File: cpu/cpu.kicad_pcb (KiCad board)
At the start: 4 copper layers, 102.4 x 40.3 mm, 39 parts, among them J2 Conn_01x08, Q3 RU1J002YN, U1 ICE40HX1K-VQ100_RV4028, U2 W25Q80DVSS, U3 AP2112K-1.2

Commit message: RAM module, many tweaks
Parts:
- Q3: value RU1J002YN -> 2N7002; footprint Package_TO_SOT_SMD:SOT-323_SC-70 -> Package_TO_SOT_SMD:SOT-23
- moved Q3 0.22 mm to (116.6, 83.4)
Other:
- board text added: "LED"
- board text added: "PROG"

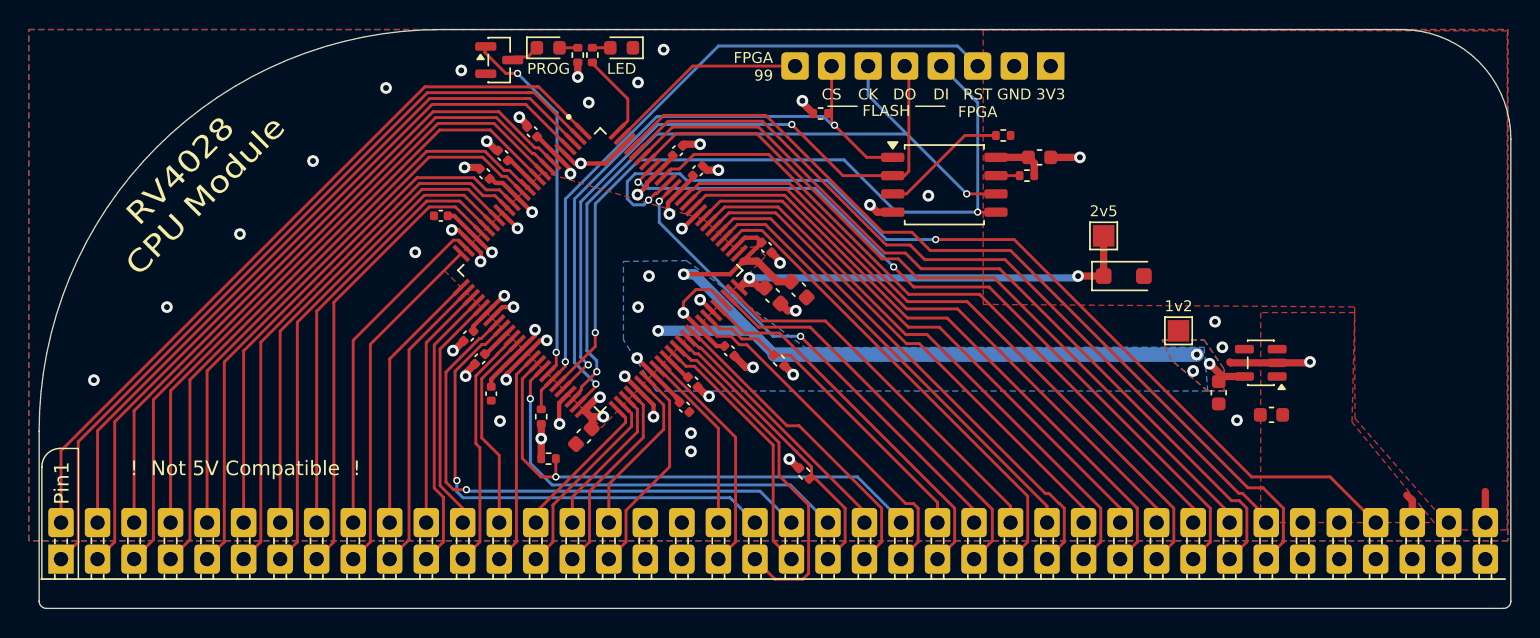
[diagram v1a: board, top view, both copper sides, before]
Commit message: Relayout CPU
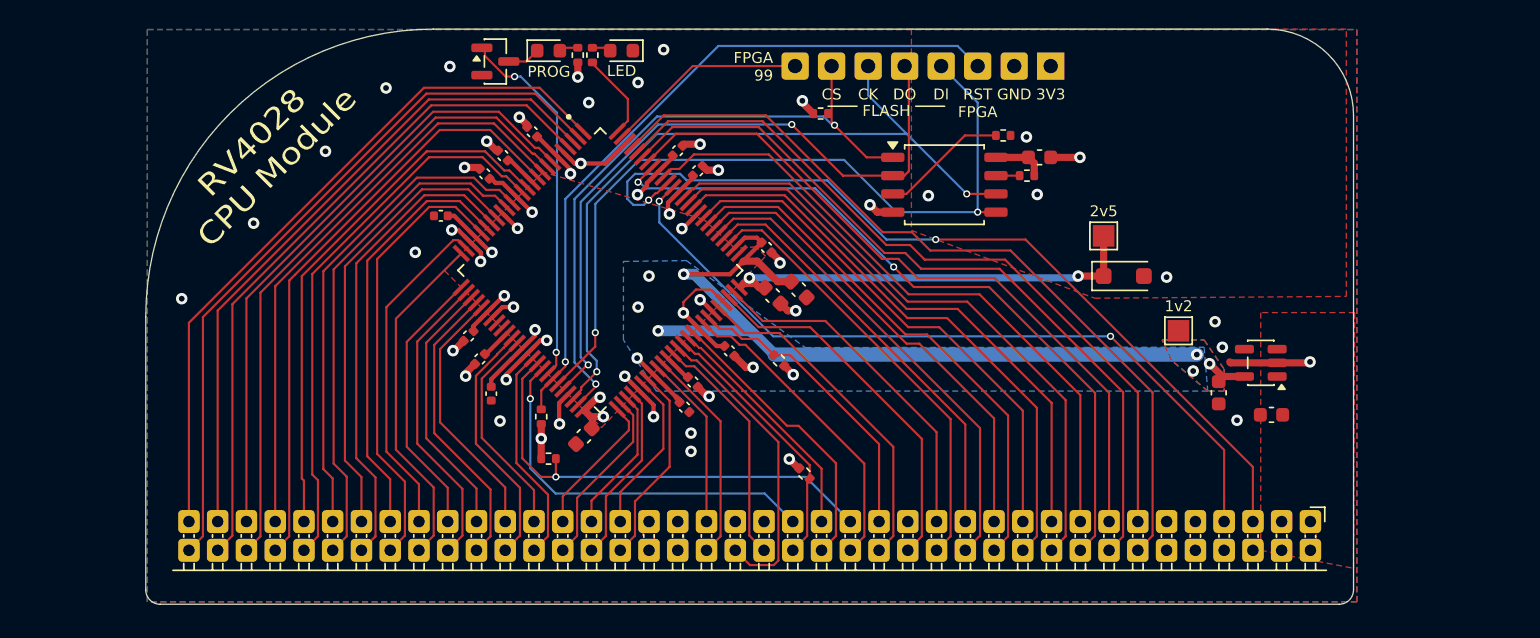
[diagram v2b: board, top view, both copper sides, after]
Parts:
- J1: footprint RV4028:ModuleHeader -> RV4028:Module_2mm
- moved J1 1.41 mm to (134.0, 117.0)
- moved Q3 0.29 mm to (116.3, 83.5)
- moved D3 0.20 mm to (120.0, 82.8)
- moved D2 0.20 mm to (125.1, 82.8)
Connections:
- J1 pad 18: unconnected-(J1-PWR-Pad18) -> +3V3
- J1 pad 40: +3V3 -> +5V
- J1 pad 58: unconnected-(J1-PWR-Pad58) -> +3V3
- J1 pad 60: ~{RST2} -> GND
- J1 pad 61: CLK2 -> GND
- J1 pad 66: SPARE1 -> GND
- J1 pad 77: SPARE2 -> SPARE1
- J1 pad 78: +5V -> SPARE2
- J1 pad 80: +3V3 -> +5V
- U1 pad 33: CLK2 -> unconnected-(U1-CLK2-Pad33)
- U1 pad 34: ~{RST2} -> unconnected-(U1-~{RST2}-Pad34)
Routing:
- net CLK2: track 37.8 -> 0.00 mm, vias 1 -> 0
- net ~{RST2}: track 34.5 -> 0.00 mm, vias 1 -> 0
- net SPARE1: track 33.9 -> 53.7 mm
- net +3V3: track 60.9 -> 53.8 mm, vias 16 -> 19
- net SPARE2: track 67.2 -> 60.8 mm
- net D7: track 61.5 -> 56.5 mm
- net D6: track 57.9 -> 53.3 mm
- net A30: track 54.7 -> 50.4 mm
- net A29: track 51.9 -> 47.8 mm
- net D5: track 54.7 -> 50.7 mm
- net D15: track 56.4 -> 52.5 mm
- net A28: track 48.6 -> 44.8 mm
- net D4: track 47.9 -> 44.1 mm
- net A31: track 53.1 -> 49.3 mm
- net ~{BUSRQ}: track 36.6 -> 32.9 mm
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- added copper zone on B.Cu, net +5V
- added copper zone on In1.Cu, net +5V
- added copper zone on In2.Cu, net +5V
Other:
- board size 102.4 x 40.3 mm -> 84 x 40 mm
- board text added: "J1"
- board text removed: "! Not 5V Compatible !"

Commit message: IO module 2mm headers
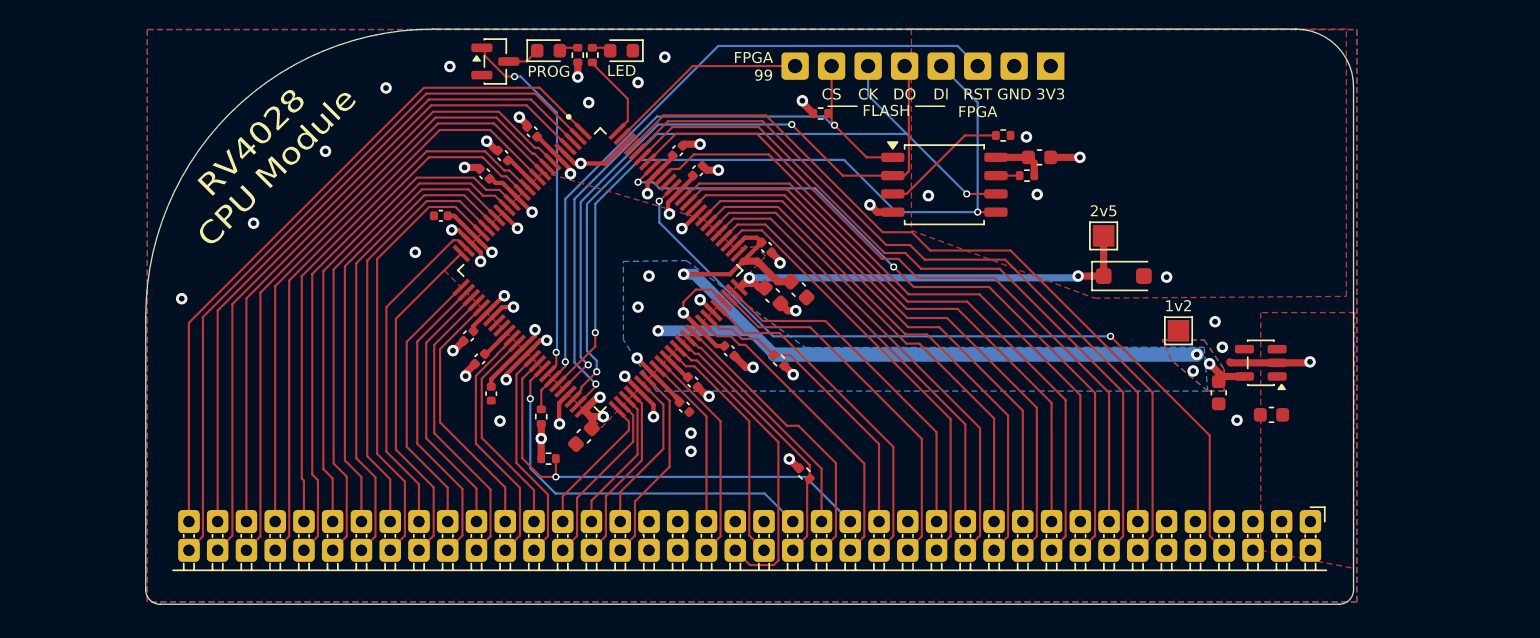
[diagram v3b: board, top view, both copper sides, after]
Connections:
- J1 pad 37: unconnected-(J1-USB_DP-Pad37) -> SPARE1
- J1 pad 77: SPARE1 -> unconnected-(J1-USB_DN-Pad77)
- J1 pad 78: SPARE2 -> unconnected-(J1-USB_DP-Pad78)
- U1 pad 90: SPARE2 -> unconnected-(U1-SPARE2-Pad90)
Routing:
- net SPARE2: track 60.8 -> 0.00 mm, vias 2 -> 0
- net SPARE1: track 53.7 -> 55.7 mm
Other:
- outline, holes or cut-outs redrawn
- board text added: "RV2048 CPU v0.1 © Mike Bell 2026 JLCJLCJLCJLC"

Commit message: RAM board attempt 2
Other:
- board text added: "RV2048 CPU v0.1 © Michael Bell 2026 JLCJLCJLCJLC"
- board text removed: "RV2048 CPU v0.1 © Mike Bell 2026 JLCJLCJLCJLC"
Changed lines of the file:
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@@
 		)
 	)
-	(gr_text "RV2048 CPU v0.1\n© Mike Bell 2026\nJLCJLCJLCJLC"
+	(gr_text "RV2048 CPU v0.1\n© Michael Bell 2026\nJLCJLCJLCJLC"
 		(at 175 101.25 90)
 		(layer "B.SilkS")

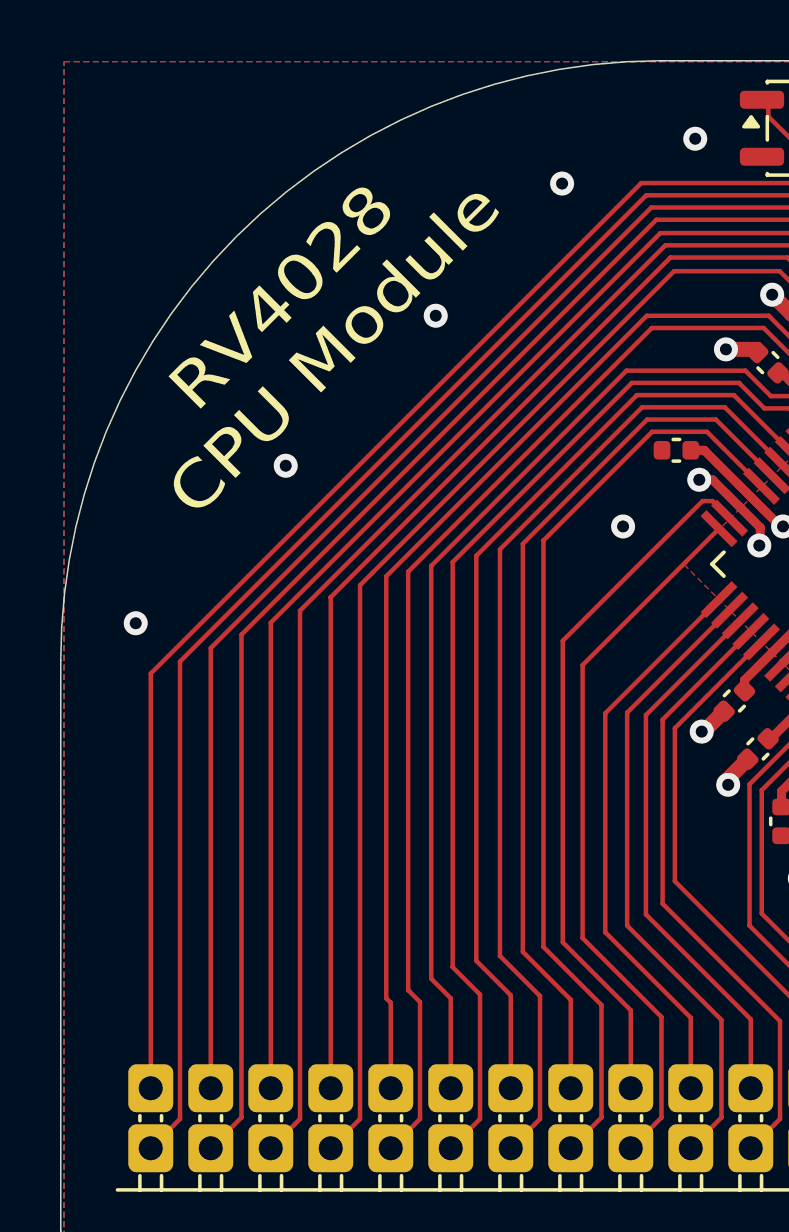
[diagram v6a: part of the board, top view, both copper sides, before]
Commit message: Finish RAM module routing
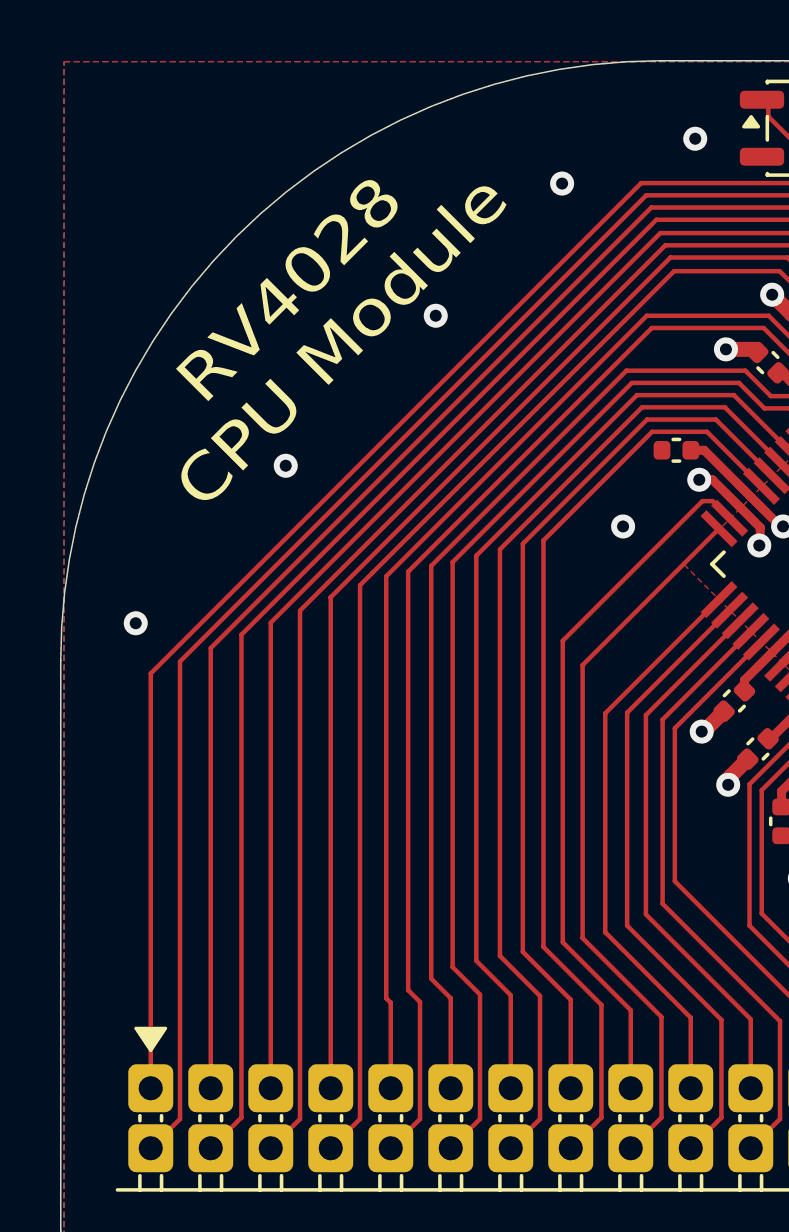
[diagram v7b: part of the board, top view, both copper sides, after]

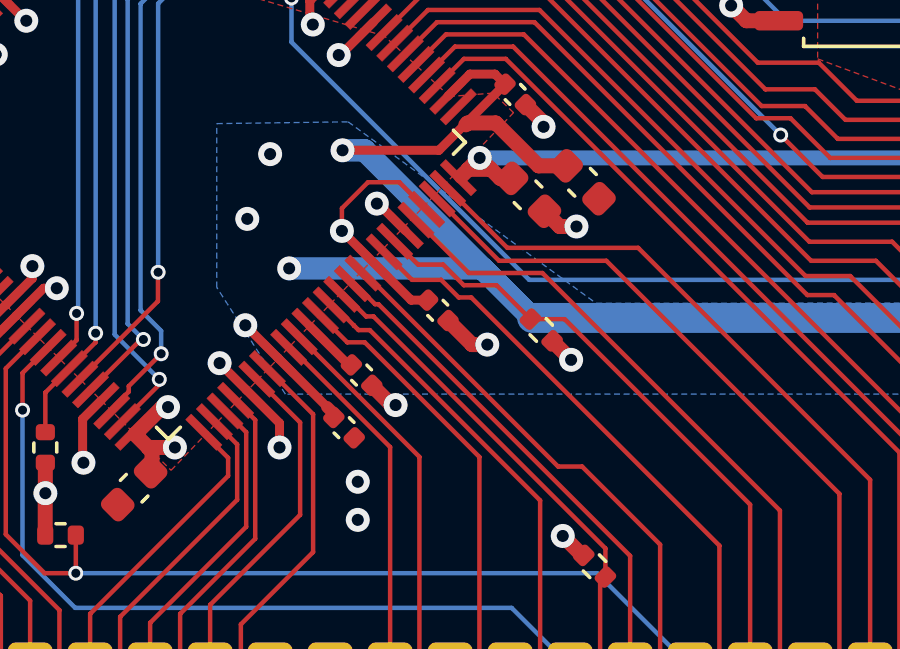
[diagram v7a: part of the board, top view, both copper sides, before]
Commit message: Pull up on REQ
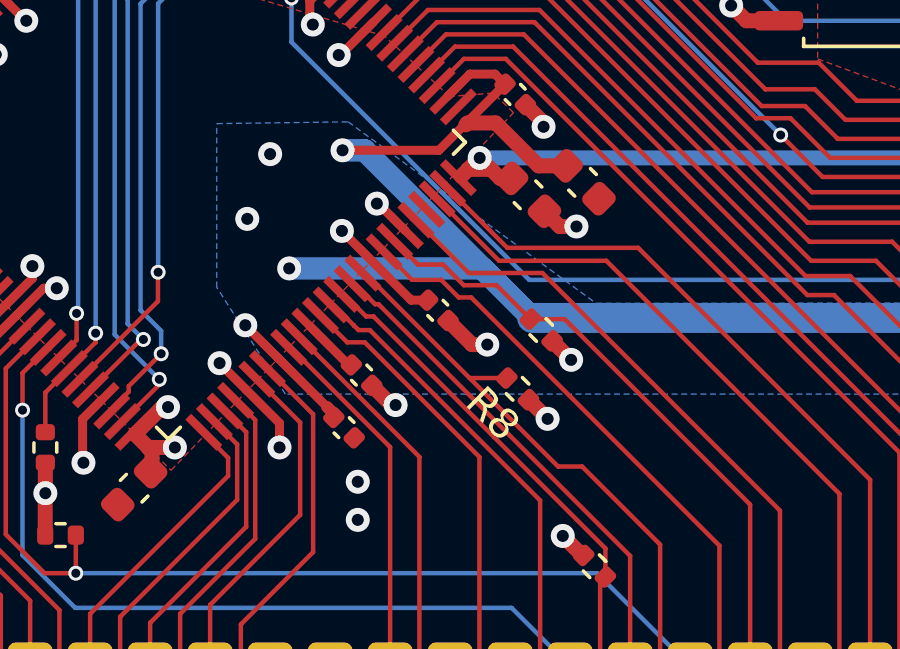
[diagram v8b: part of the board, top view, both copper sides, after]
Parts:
- added R8: 10k, Resistor_SMD:R_0402_1005Metric, F.Cu at (135.2, 106.2)
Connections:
- U1 pad 72: +3V3 -> unconnected-(U1-NC-Pad72)
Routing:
- net +3V3: track 53.5 -> 50.1 mm, vias 19 -> 20
- net ~{REQ}: track 20.1 -> 21.4 mm
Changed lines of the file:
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@@
 	(net 91 "unconnected-(U1-~{RST2}-Pad34)")
 	(net 92 "unconnected-(U1-SPARE2-Pad90)")
+	(net 93 "unconnected-(U1-NC-Pad72)")
 	(footprint "Package_TO_SOT_SMD:SOT-23"
 		(layer "F.Cu")
@@
 			(layers "F.Cu" "F.Mask" "F.Paste")
 			(roundrect_rratio 0.035)
-			(net 1 "+3V3")
+			(net 93 "unconnected-(U1-NC-Pad72)")
 			(pinfunction "NC")
-			(pintype "free")
+			(pintype "free+no_connect")
 			(solder_mask_margin 0.102)
 		)
@@
 	(footprint "Resistor_SMD:R_0402_1005Metric"
 		(layer "F.Cu")
+		(at 135.25 106.25 135)
+		(descr "Resistor SMD 0402 (1005 Metric), square (rectangular) end terminal, IPC-7351 nominal, (Body size source: IPC-SM-782 page 72, https://www.pcb-3d.com/wordpress/wp-content/uploads/ipc-sm-782a_amendment_1_and_2.pdf), generated with kicad-footprint-generator")
+		(tags "resistor")
+		(property "Reference" "R8"
+			(at 0 -1.17 135)
+			(layer "F.SilkS")
+			(effects
+				(font
+					(size 1 1)
+					(thickness 0.15)
+				)
+			)
+		)
+		(property "Value" "10k"
+			(at 0 1.17 135)
+			(layer "F.Fab")
+			(effects
+				(font
+					(size 1 1)
+					(thickness 0.15)
+				)
+			)
+		)
+		(property "Datasheet" "~"
+			(at 0 0 135)
+			(layer "F.Fab")
+			(hide yes)
+			(effects
+				(font
+					(size 1.27 1.27)
+					(thickness 0.15)
+				)
+			)
+		)
+		(property "Description" "Resistor"
+			(at 0 0 135)
+			(layer "F.Fab")
+			(hide yes)
+			(effects
+				(font
+					(size 1.27 1.27)
+					(thickness 0.15)
+				)
+			)
+		)
+		(property "JLC" "C25744"
+			(at 0 0 135)
+			(unlocked yes)
+			(layer "F.Fab")
+			(hide yes)
+			(effects
+				(font
+					(size 1 1)
+					(thickness 0.15)
+				)
+			)
+		)
+		(property ki_fp_filters "R_*")
+		(sheetname "/")
+		(sheetfile "cpu.kicad_sch")
+		(attr smd)
+		(fp_line
+			(start -0.153641 -0.38)
+			(end 0.153641 -0.38)
+			(stroke
+				(width 0.12)
+				(type solid)
+			)
+			(layer "F.SilkS")
+		)
+		(fp_line
+			(start -0.153641 0.38)
+			(end 0.153641 0.38)
+			(stroke
+				(width 0.12)
+				(type solid)
+			)
+			(layer "F.SilkS")
+		)
+		(fp_line
+			(start 0.93 -0.47)
+			(end 0.93 0.47)
+			(stroke
+				(width 0.05)
+				(type solid)
+			)
+			(layer "F.CrtYd")
+		)
+		(fp_line
+			(start 0.93 0.47)
+			(end -0.93 0.47)
+			(stroke
+				(width 0.05)
+				(type solid)
+			)
+			(layer "F.CrtYd")
+		)
+		(fp_line
+			(start -0.93 -0.47)
+			(end 0.93 -0.47)
+			(stroke
+				(width 0.05)
+				(type solid)
+			)
+			(layer "F.CrtYd")
+		)
+		(fp_line
+			(start -0.93 0.47)
+			(end -0.93 -0.47)
+			(stroke
+				(width 0.05)
+				(type solid)
+			)
+			(layer "F.CrtYd")
+		)
+		(fp_line
+			(start 0.525 -0.27)
+			(end 0.525 0.27)
+			(stroke
+				(width 0.1)
+				(type solid)
+			)
+			(layer "F.Fab")
+		)
+		(fp_line
+			(start 0.525 0.27)
+			(end -0.525 0.27)
+			(stroke
+				(width 0.1)
+				(type solid)
+			)
+			(layer "F.Fab")
+		)
+		(fp_line
+			(start -0.525 -0.27)
+			(end 0.525 -0.27)
+			(stroke
+				(width 0.1)
+				(type solid)
+			)
+			(layer "F.Fab")
+		)
+		(fp_line
+			(start -0.525 0.27)
+			(end -0.525 -0.27)
+			(stroke
+				(width 0.1)
+				(type solid)
+			)
+			(layer "F.Fab")
+		)
+		(fp_text user "${REFERENCE}"
+			(at 0 0 135)
+			(layer "F.Fab")
+			(effects
+				(font
+					(size 0.26 0.26)
+					(thickness 0.04)
+				)
+			)
+		)
+		(pad "1" smd roundrect
+			(at -0.509999 0 135)
+			(size 0.54 0.64)
+			(layers "F.Cu" "F.Mask" "F.Paste")
+			(roundrect_rratio 0.25)
+			(net 1 "+3V3")
+			(pintype "passive")
+		)
+		(pad "2" smd roundrect
+			(at 0.509999 0 135)
+			(size 0.54 0.64)
+			(layers "F.Cu" "F.Mask" "F.Paste")
+			(roundrect_rratio 0.25)
+			(net 76 "~{REQ}")
+			(pintype "passive")
+		)
+		(embedded_fonts no)
+		(model "${KICAD9_3DMODEL_DIR}/Resistor_SMD.3dshapes/R_0402_1005Metric.step"
+			(offset
+				(xyz 0 0 0)
+			)
+			(scale
+				(xyz 1 1 1)
+			)
+			(rotate
+				(xyz 0 0 0)
+			)
+		)
+	)
+	(footprint "Resistor_SMD:R_0402_1005Metric"
+		(layer "F.Cu")
 		(at 138.938 87.122)
 		(descr "Resistor SMD 0402 (1005 Metric), square (rectangular) end terminal, IPC-7351 nominal, (Body size source: IPC-SM-782 page 72, https://www.pcb-3d.com/wordpress/wp-content/uploads/ipc-sm-782a_amendment_1_and_2.pdf), generated with kicad-footprint-generator")
@@
 	)
 	(segment
-		(start 129.392723 100.232074)
-		(end 129.392723 100.985277)
-		(width 0.15)
-		(layer "F.Cu")
-		(net 1)
-	)
-	(segment
 		(start 113.449056 94.234)
 		(end 113.002 94.234)
@@
 	)
 	(segment
-		(start 130.261704 99.363093)
-		(end 129.392723 100.232074)
-		(width 0.15)
-		(layer "F.Cu")
-		(net 1)
-	)
-	(segment
-		(start 131.306073 99.363093)
-		(end 130.261704 99.363093)
-		(width 0.15)
-		(layer "F.Cu")
-		(net 1)
-	)
-	(segment
 		(start 115.003378 95.788322)
 		(end 113.449056 94.234)
@@
 	)
 	(segment
+		(start 136.25 107.25)
+		(end 135.610624 106.610624)
+		(width 0.5)
+		(layer "F.Cu")
+		(net 1)
+	)
+	(segment
 		(start 119.507 109.728)
 		(end 119.507 108.714)
@@
 	)
 	(segment
-		(start 132.214358 100.271378)
-		(end 131.306073 99.363093)
-		(width 0.15)
-		(layer "F.Cu")
-		(net 1)
-	)
-	(segment
 		(start 121.539 91.010234)
 		(end 121.539 91.313)
@@
 		(net 1)
 	)
+	(via
+		(at 136.25 107.25)
+		(size 0.8)
+		(drill 0.4)
+		(layers "F.Cu" "B.Cu")
+		(free yes)
+		(net 1)
+	)
 	(segment
 		(start 136.114641 97.514559)
@@
 	)
 	(segment
-		(start 130.152153 102.392699)
+		(start 134.889376 105.889376)
+		(end 133.64883 105.889376)
+		(width 0.15)
+		(layer "F.Cu")
+		(net 76)
+	)
+	(segment
+		(start 133.64883 105.889376)
 		(end 136.598454 108.839)
 		(width 0.15)
@@
 		(width 0.15)
 		(layer "F.Cu")
+		(net 76)
+	)
+	(segment
+		(start 130.152153 102.392699)
+		(end 133.64883 105.889376)
+		(width 0.15)
+		(layer "F.Cu")
